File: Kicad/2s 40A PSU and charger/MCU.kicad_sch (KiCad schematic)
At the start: 14 parts, among them J12 USB, U5 THVD1420DRLR, U6 CH32X035G8U6

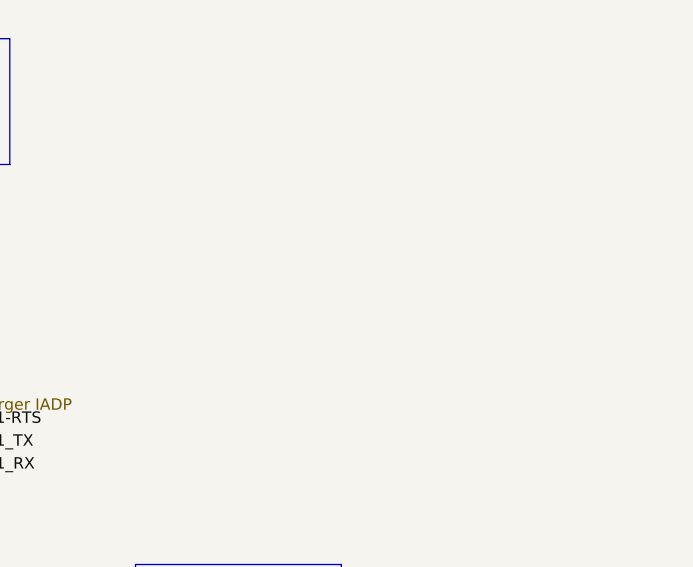
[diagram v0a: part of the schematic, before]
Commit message: Finished routing PSU
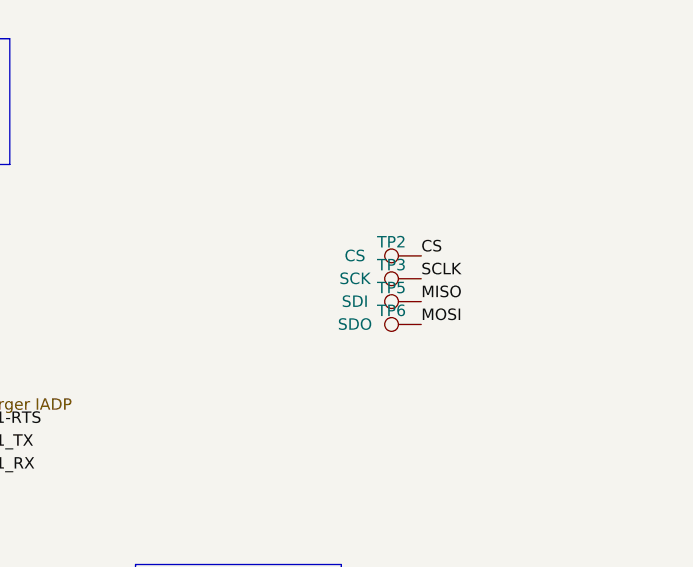
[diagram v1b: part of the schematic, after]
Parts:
- added TP2: CS, TestPoint:TestPoint_Pad_D1.0mm, symbol Connector:TestPoint
- added TP3: SCK, TestPoint:TestPoint_Pad_D1.0mm, symbol Connector:TestPoint
- added TP5: SDI, TestPoint:TestPoint_Pad_D1.0mm, symbol Connector:TestPoint
- added TP6: SDO, TestPoint:TestPoint_Pad_D1.0mm, symbol Connector:TestPoint
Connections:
- net CS: now also TP2.1
- net MISO: now also TP5.1
- net MOSI: now also TP6.1
- net SCLK: now also TP3.1

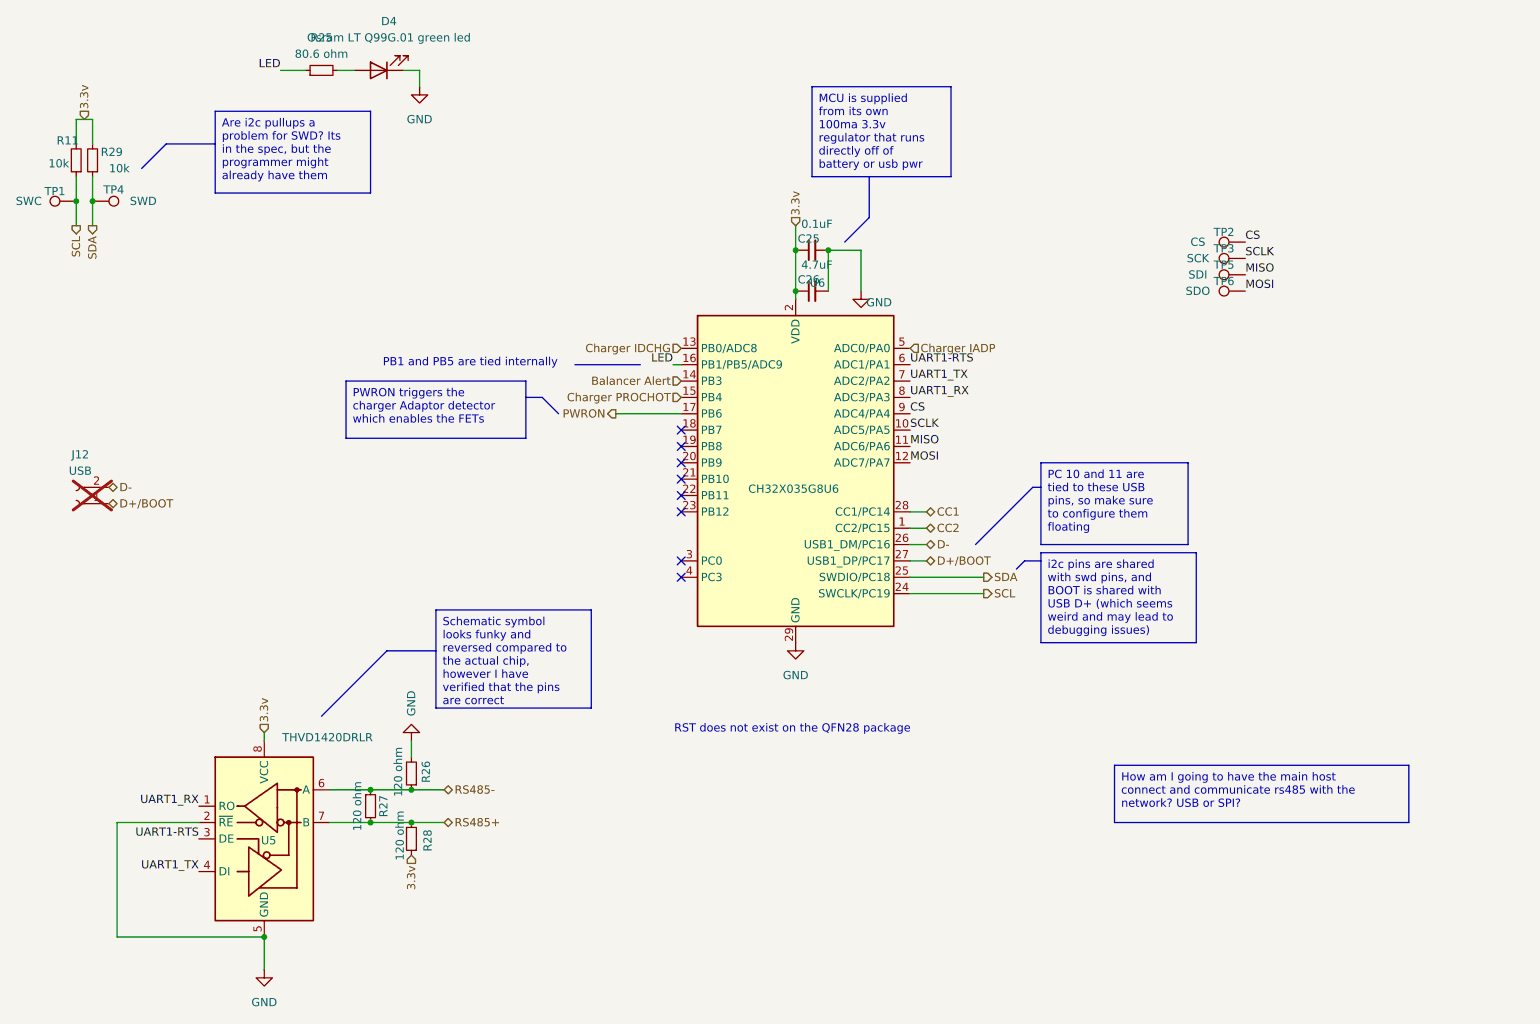
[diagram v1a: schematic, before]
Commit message: Final tweaks, capacitor placement and GND keepouts
I tried my best to isolate signal grounds from the power paths. I also added a bunch of ground keepouts to help isolate.
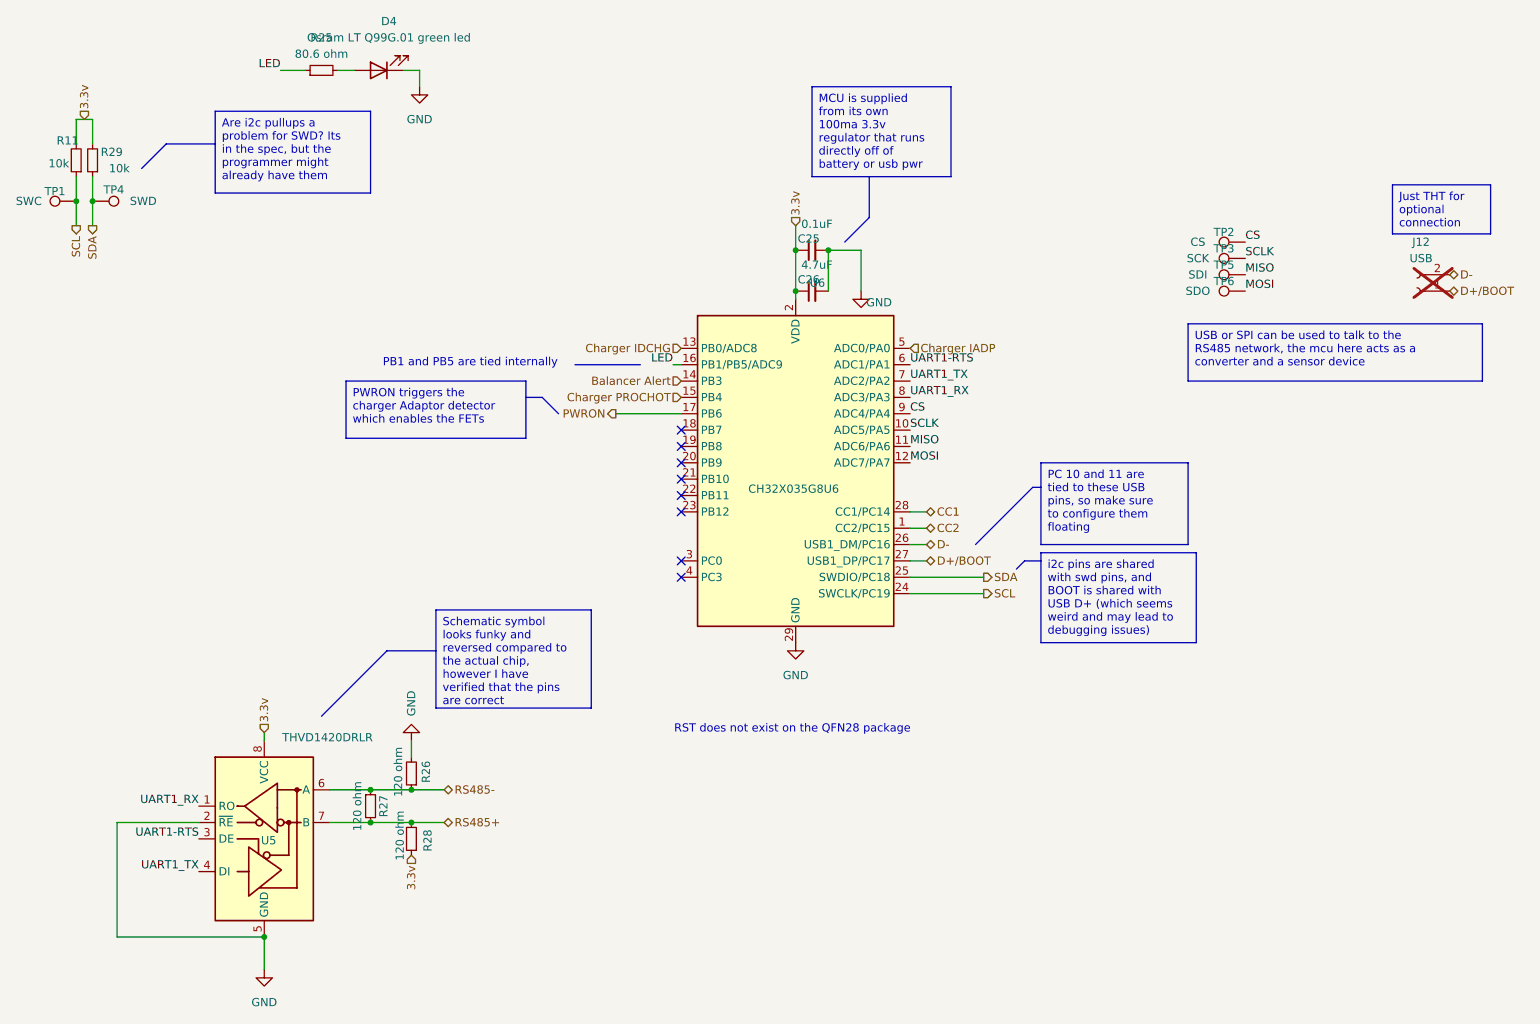
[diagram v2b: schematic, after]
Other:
- moved on the sheet: J12
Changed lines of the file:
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@@
 	(title_block
 		(title "CACKLE 2s 40A PSU & Charger")
-		(date "2024-12-01")
+		(date "2024-12-23")
 		(rev "V1")
 		(company "ME")
@@
 		)
 	)
-	(text_box "How am I going to have the main host connect and communicate rs485 with the network? USB or SPI?"
-		(exclude_from_sim no)
-		(at 190.5 138.43 0)
+	(text_box "USB or SPI can be used to talk to the RS485 network, the mcu here acts as a converter and a sensor device"
+		(exclude_from_sim no)
+		(at 201.93 69.85 0)
 		(size 45.72 8.89)
+		(stroke
+			(width 0)
+			(type default)
+		)
+		(fill
+			(type none)
+		)
+		(effects
+			(font
+				(size 1.27 1.27)
+			)
+			(justify left top)
+		)
+	)
+	(text_box "Just THT for optional connection"
+		(exclude_from_sim no)
+		(at 233.68 48.26 0)
+		(size 15.24 7.62)
 		(stroke
 			(width 0)
@@
 	(hierarchical_label "D+{slash}BOOT"
 		(shape bidirectional)
-		(at 34.29 97.79 0)
+		(at 242.57 64.77 0)
 		(fields_autoplaced yes)
 		(effects
@@
 	(hierarchical_label "D-"
 		(shape bidirectional)
-		(at 34.29 95.25 0)
+		(at 242.57 62.23 0)
 		(fields_autoplaced yes)
 		(effects
@@
 	(symbol
 		(lib_id "Connector:Conn_01x02_Socket")
-		(at 29.21 97.79 180)
+		(at 237.49 64.77 180)
 		(unit 1)
 		(exclude_from_sim no)
@@
 		(fields_autoplaced yes)
 		(property "Reference" "J12"
-			(at 29.845 90.17 0)
+			(at 238.125 57.15 0)
 			(effects
 				(font
@@
 		)
 		(property "Value" "USB"
-			(at 29.845 92.71 0)
+			(at 238.125 59.69 0)
 			(effects
 				(font
@@
 		)
 		(property "Footprint" "Connector_PinHeader_1.27mm:PinHeader_1x02_P1.27mm_Vertical"
-			(at 29.21 97.79 0)
+			(at 237.49 64.77 0)
 			(effects
 				(font
@@
 		)
 		(property "Datasheet" "~"
-			(at 29.21 97.79 0)
+			(at 237.49 64.77 0)
 			(effects
 				(font
@@
 		)
 		(property "Description" "Generic connector, single row, 01x02, script generated"
-			(at 29.21 97.79 0)
-			(effects
-				(font
+			(at 237.49 64.77 0)
+			(effects
+				(font

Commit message: Added LCSC part numbers, DNP attr, and exported Gerbers
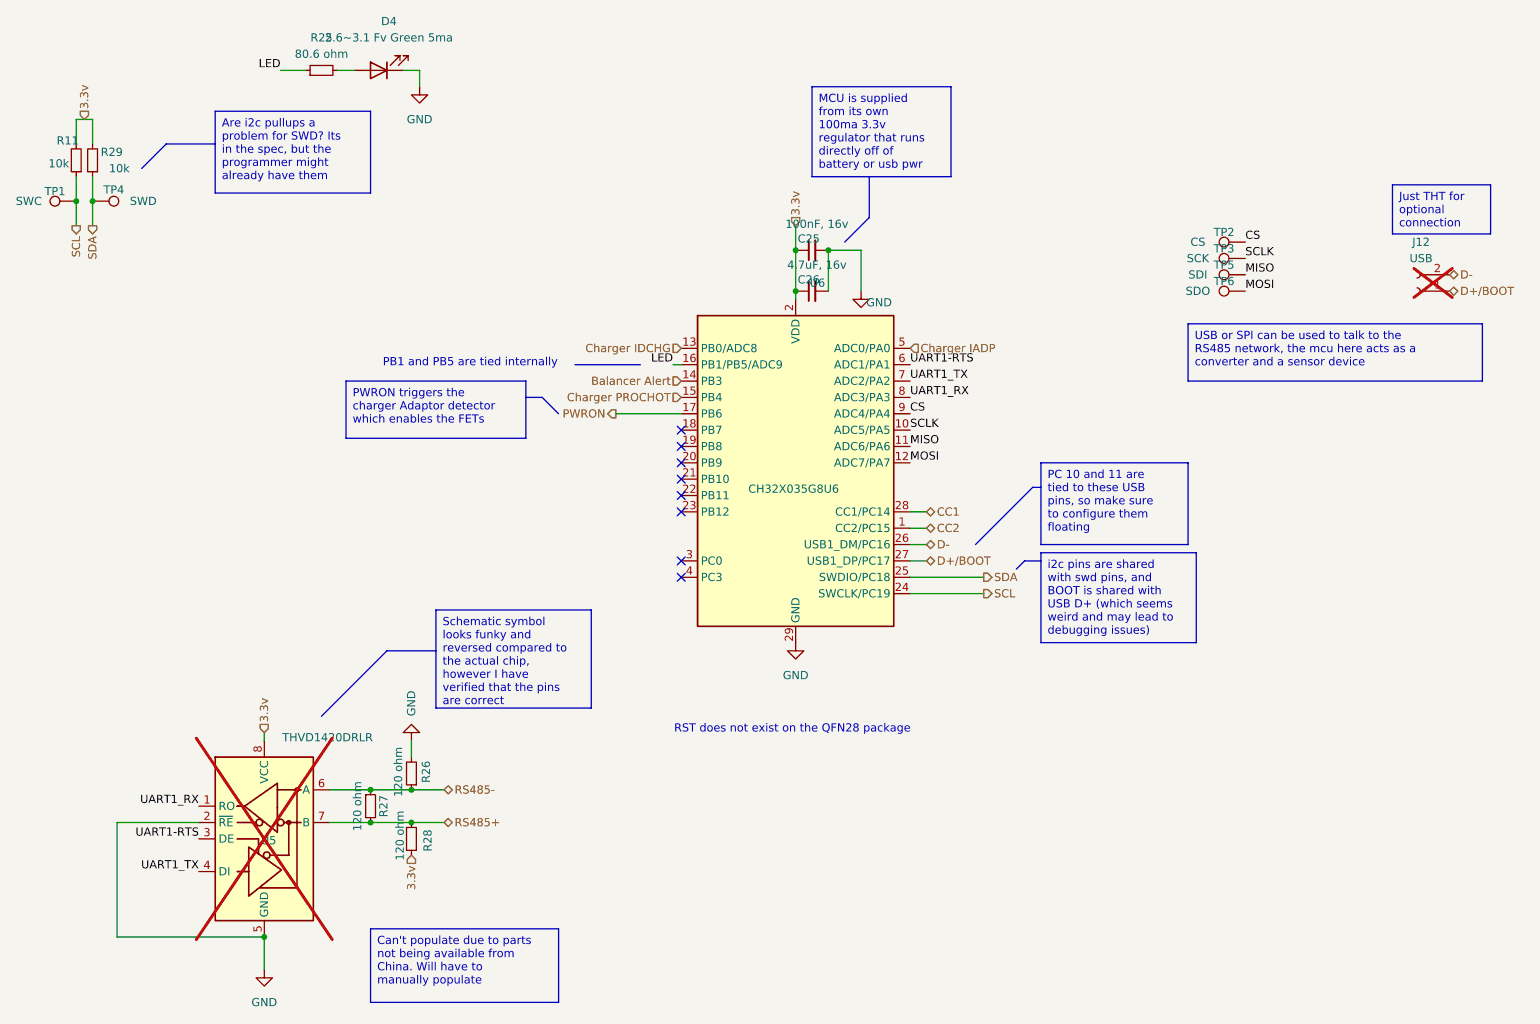
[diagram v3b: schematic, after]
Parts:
- C25: value 0.1uF -> 100nF, 16v; LCSC (none) -> C1525
- C26: value 4.7uF -> 4.7uF, 16v; LCSC (none) -> C19666
- D4: value Osram LT Q99G.01 green led -> 2.6~3.1 Fv Green 5ma; LCSC (none) -> C3028858
- R11, R29: LCSC (none) -> C25744
- U5: now not fitted
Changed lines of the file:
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@@
+		)
+	)
+	(text_box "Can't populate due to parts not being available from China. Will have to manually populate"
+		(exclude_from_sim no)
+		(at 74.93 163.83 0)
+		(size 29.21 11.43)
+		(stroke
+			(width 0)
+			(type default)
+		)
+		(fill
+			(type none)
+		)
+		(effects
+			(font
+				(size 1.27 1.27)
+			)
+			(justify left top)
 		)
 	)
@@
 			)
 		)
-		(property "Value" "Osram LT Q99G.01 green led"
+		(property "Value" "2.6~3.1 Fv Green 5ma"
 			(at 77.7875 25.4 0)
 			(effects
@@
 		)
 		(property "Description" "Light emitting diode"
+			(at 76.2 30.48 0)
+			(effects
+				(font
+					(size 1.27 1.27)
+				)
+				(hide yes)
+			)
+		)
+		(property "LCSC" "C3028858"
 			(at 76.2 30.48 0)
 			(effects
@@
 			)
 		)
+		(property "LCSC" "C25744"
+			(at 26.162 41.402 0)
+			(effects
+				(font
+					(size 1.27 1.27)
+				)
+				(hide yes)
+			)
+		)
 		(pin "1"
 		)
@@
 			)
 		)
-		(property "Value" "0.1uF"
+		(property "Value" "100nF, 16v"
 			(at 144.272 54.356 90)
 			(effects
@@
 		(property "Description" "Unpolarized capacitor, small symbol"
 			(at 143.51 58.42 0)
+			(effects
+				(font
+					(size 1.27 1.27)
+				)
+				(hide yes)
+			)
+		)
+		(property "LCSC" "C1525"
+			(at 143.002 56.642 0)
 			(effects
 				(font
@@
 		(in_bom yes)
 		(on_board yes)
-		(dnp no)
+		(dnp yes)
 		(property "Reference" "U5"
 			(at 57.912 150.114 0)
@@
 			)
 		)
+		(property "LCSC" "C25744"
+			(at 33.02 43.18 0)
+			(effects
+				(font
+					(size 1.27 1.27)
+				)
+				(hide yes)
+			)
+		)
 		(pin "1"
 		)
@@
 			)
 		)
-		(property "Value" "4.7uF"
+		(property "Value" "4.7uF, 16v"
 			(at 144.272 60.706 90)
 			(effects
@@
 			(effects
 				(font
+					(size 1.27 1.27)
+				)
+				(hide yes)
+			)
+		)
+		(property "LCSC" "C19666"
+			(at 143.002 62.992 0)
+			(effects
+				(font

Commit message: Fixed Current sense resistor footprints, adjusted current GND blocks
I had to source alternative resistors and change the footprints as well. I didn't realize though that the 2818 footprint I had was wrong though, 2816 is not quite compatible!

Another thing I did was fix gnd guides and added horse shoe shapes around the sensitive component vias.
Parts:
- R25: LCSC (none) -> C185392
- R26, R27, R28: LCSC (none) -> C25079
- U6: LCSC (none) -> C7437027
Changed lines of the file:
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@@
+			)
+		)
+		(property "LCSC" "C25079"
+			(at 76.962 144.78 0)
+			(effects
+				(font
+					(size 1.27 1.27)
+				)
+				(hide yes)
 			)
 		)
@@
 		(property "Description" "Resistor, small symbol"
 			(at 81.28 139.7 0)
+			(effects
+				(font
+					(size 1.27 1.27)
+				)
+				(hide yes)
+			)
+		)
+		(property "LCSC" "C25079"
+			(at 83.566 139.446 0)
 			(effects
 				(font
@@
 			)
 		)
+		(property "LCSC" "C185392"
+			(at 67.31 25.4 0)
+			(effects
+				(font
+					(size 1.27 1.27)
+				)
+				(hide yes)
+			)
+		)
 		(pin "1"
 		)
@@
 			)
 		)
+		(property "LCSC" "C7437027"
+			(at 143.1641 63.5 0)
+			(effects
+				(font
+					(size 1.27 1.27)
+				)
+				(hide yes)
+			)
+		)
 		(pin "9"
 		)
@@
 			(effects
 				(font
+					(size 1.27 1.27)
+				)
+				(hide yes)
+			)
+		)
+		(property "LCSC" "C25079"
+			(at 83.82 150.114 0)
+			(effects
+				(font
